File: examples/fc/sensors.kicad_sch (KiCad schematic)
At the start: 8 parts, among them U4 MPU-6000, U5 W25Q128JVS

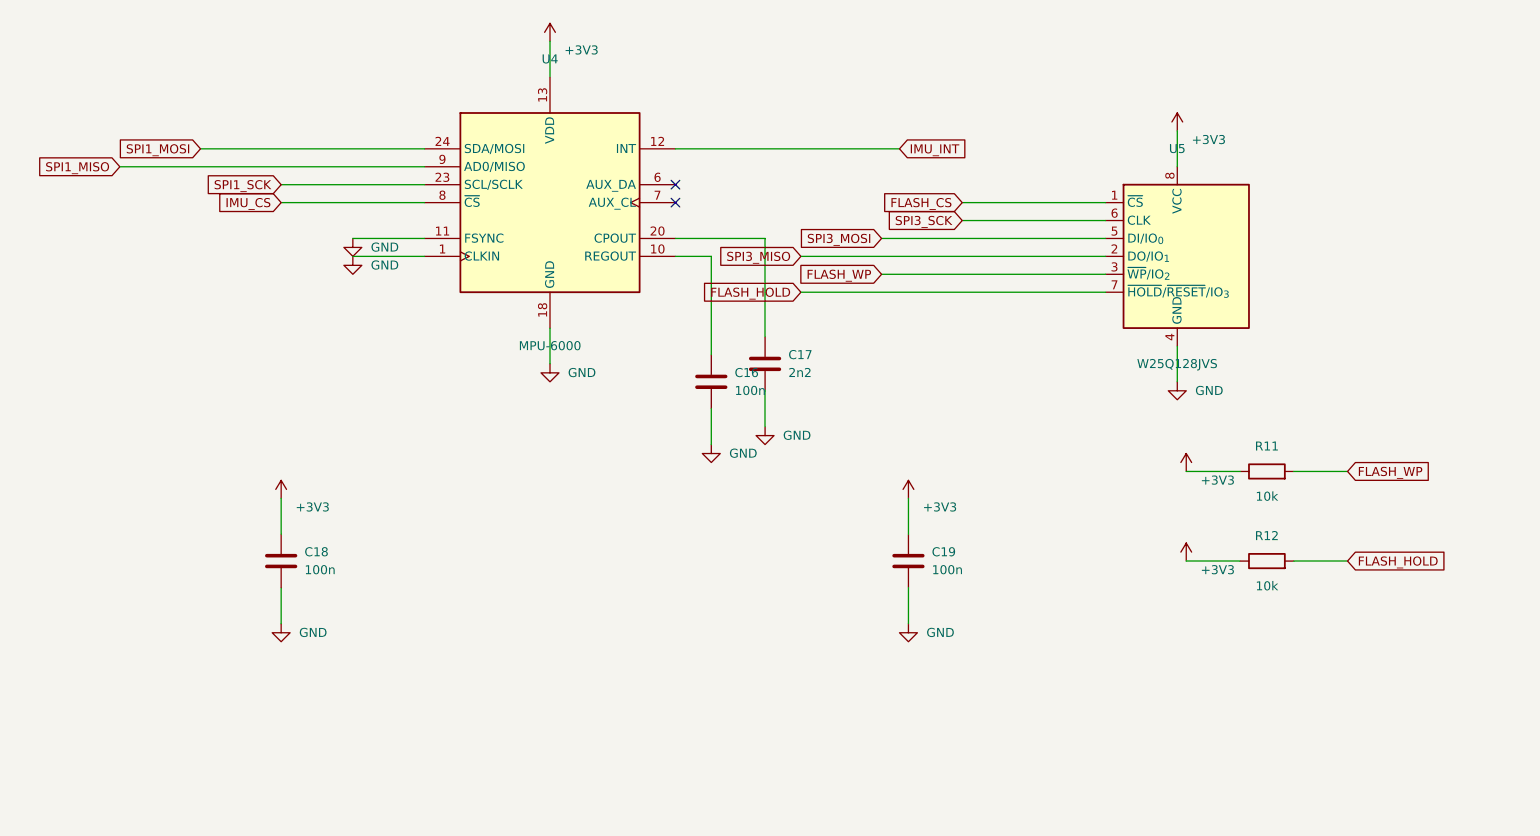
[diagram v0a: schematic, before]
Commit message: Add structured schematic scenes and fix example overlaps
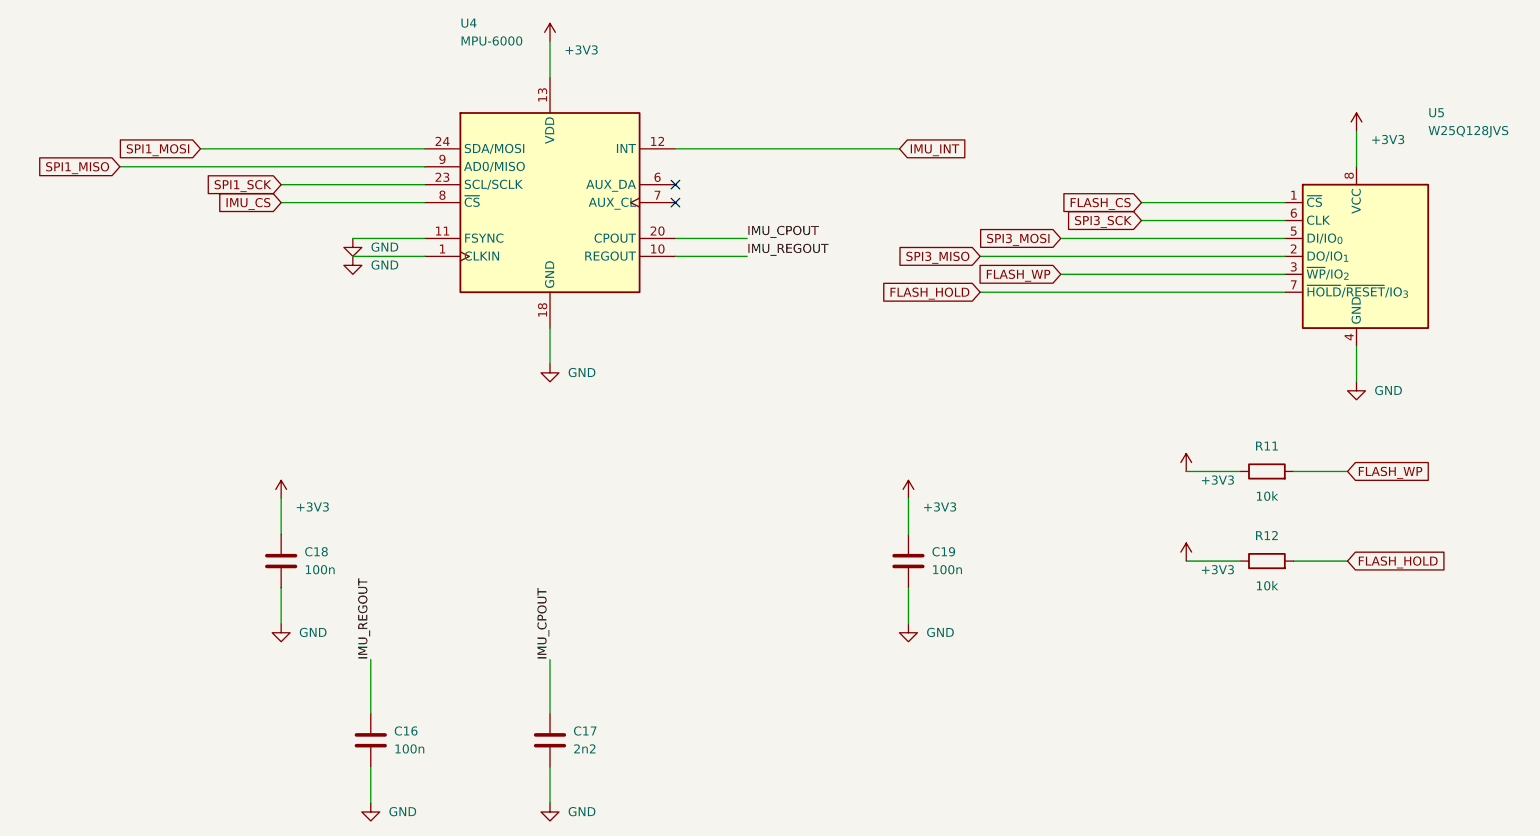
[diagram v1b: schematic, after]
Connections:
- net IMU_REGOUT: now reaches C16.1, U4.10 (REGOUT)
- net IMU_CPOUT: now reaches C17.1, U4.20 (CPOUT)
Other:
- moved on the sheet: C16, C17, U5
